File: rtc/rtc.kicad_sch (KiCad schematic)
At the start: 14 parts, among them J1 Conn_02x03_Odd_Even, J2 Conn_01x04, J3 Conn_01x04, J4 Conn_01x04, U1 PCF8563T/5_518, Y1 LFXTAL016178REEL

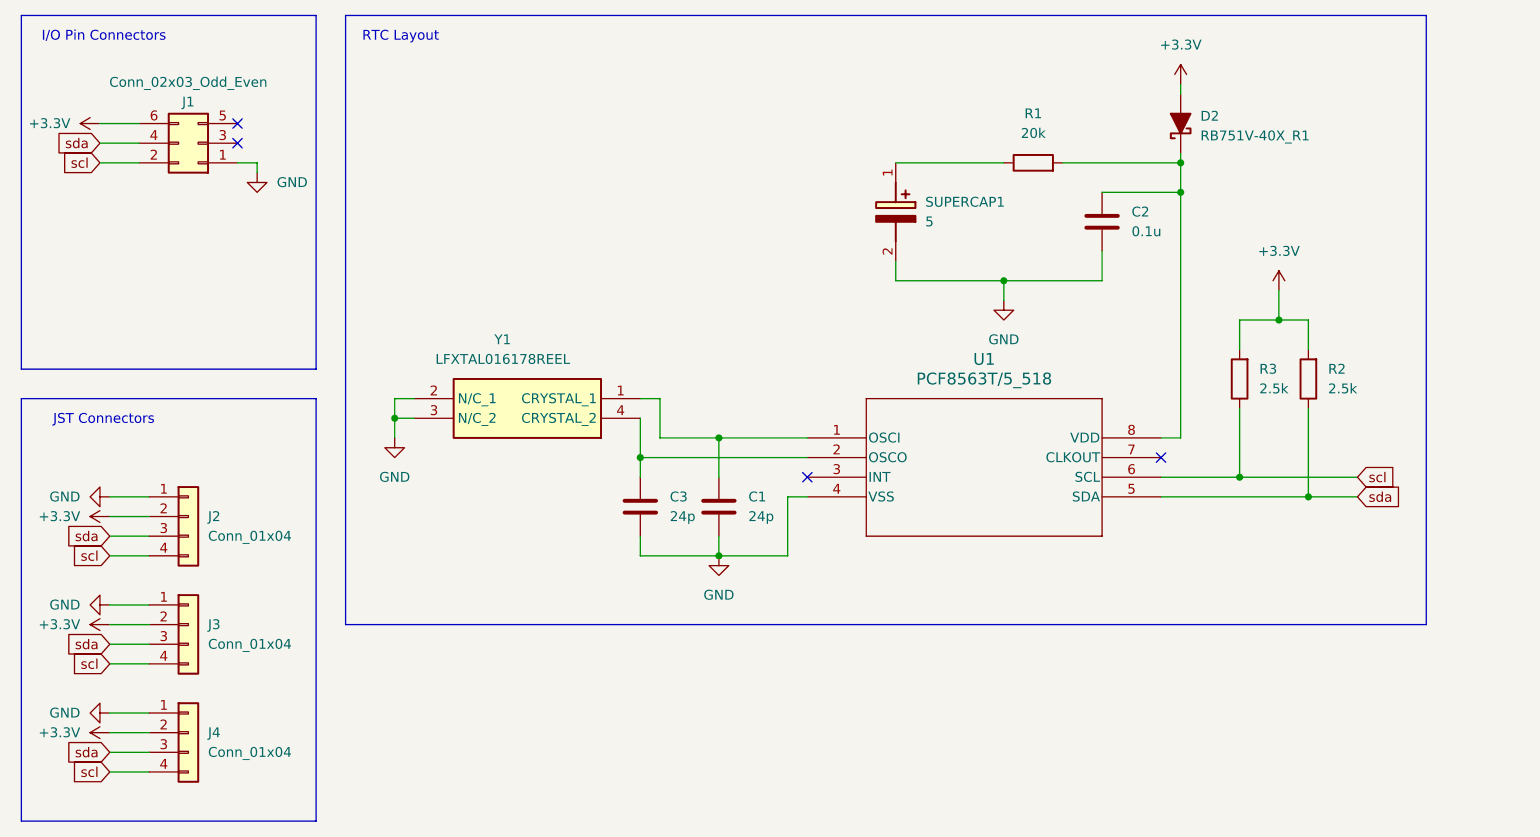
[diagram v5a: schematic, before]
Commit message: finished rtc board + sensor base 3d model change
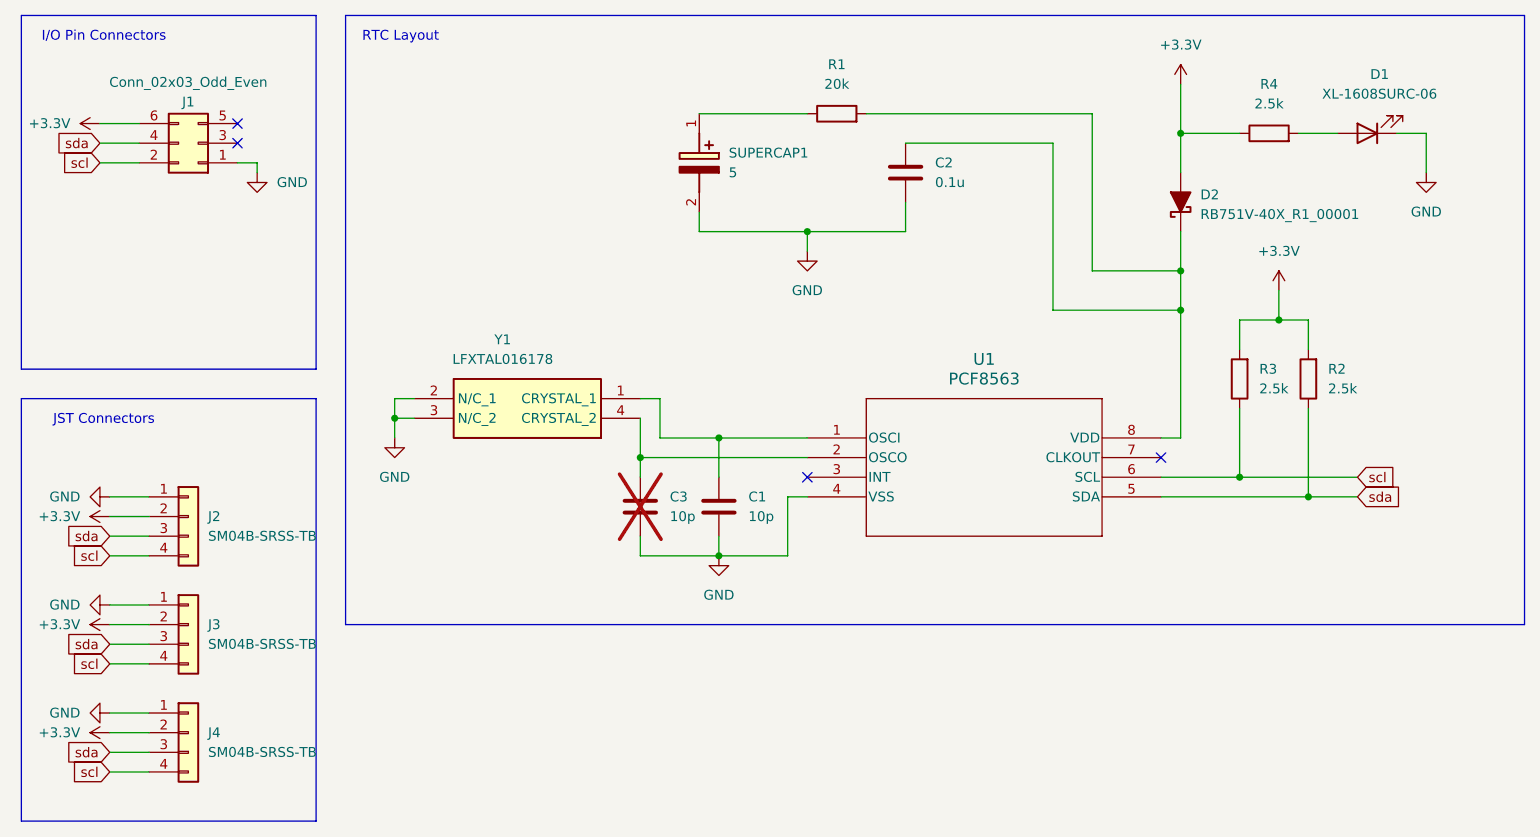
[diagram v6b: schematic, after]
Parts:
- added D1: XL-1608SURC-06, LED_SMD:LED_0603_1608Metric_Pad1.05x0.95mm_HandSolder, symbol Device:LED
- added R4: 2.5k, Resistor_SMD:R_0603_1608Metric_Pad0.98x0.95mm_HandSolder, symbol Device:R
- C1: value 24p -> 10p; footprint Capacitor_SMD:C_0402_1005Metric_Pad0.74x0.62mm_HandSolder -> Capacitor_SMD:C_0603_1608Metric_Pad1.08x0.95mm_HandSolder; Manufacturer Name (none) -> HRE; Manufacturer Part Number (none) -> CGA0603C0G100J500JT; Supplier Name (none) -> LCSC; Supplier Part Number (none) -> C45359928
- C2: footprint Capacitor_SMD:C_0402_1005Metric_Pad0.74x0.62mm_HandSolder -> Capacitor_SMD:C_0603_1608Metric_Pad1.08x0.95mm_HandSolder; Manufacturer Name (none) -> HRE; Manufacturer Part Number (none) -> CGA0603X7R104K500JT; Supplier Name (none) -> LCSC; Supplier Part Number (none) -> C6119867
- C3: value 24p -> 10p; footprint Capacitor_SMD:C_0402_1005Metric_Pad0.74x0.62mm_HandSolder -> Capacitor_SMD:C_0603_1608Metric_Pad1.08x0.95mm_HandSolder; Manufacturer Name (none) -> HRE; Manufacturer Part Number (none) -> CGA0603C0G100J500JT; Supplier Name (none) -> LCSC; Supplier Part Number (none) -> C45359928; now not fitted
- D2: value RB751V-40X_R1 -> RB751V-40X_R1_00001; Manufacturer Name (none) -> Panjit International Inc.; Manufacturer Part Number (none) -> RB751V-40X_R1_00001; Supplier Name (none) -> Digikey; Supplier Part Number (none) -> 3757-RB751V-40X_R1_00001CT-ND
- J1: now left out of the parts list
- J2, J3, J4: value Conn_01x04 -> SM04B-SRSS-TB; Manufacturer Name (none) -> XYECONN; Manufacturer Part Number (none) -> XY-SM04B-SRSS-TB; Supplier Name (none) -> LCSC; Supplier Part Number (none) -> C51940130
- R1: footprint Resistor_SMD:R_0402_1005Metric_Pad0.72x0.64mm_HandSolder -> Resistor_SMD:R_0603_1608Metric_Pad0.98x0.95mm_HandSolder; Manufacturer Name (none) -> FOJAN; Manufacturer Part Number (none) -> FRQ0603F2002TS; Supplier Name (none) -> LCSC; Supplier Part Number (none) -> C7468442
- R2, R3: footprint Resistor_SMD:R_0402_1005Metric_Pad0.72x0.64mm_HandSolder -> Resistor_SMD:R_0603_1608Metric_Pad0.98x0.95mm_HandSolder; Manufacturer Name (none) -> FOJAN; Manufacturer Part Number (none) -> FRC0603F2551TS; Substitutional Values (none) -> 2.55k; Supplier Name (none) -> LCSC; Supplier Part Number (none) -> C2933178
- SUPERCAP1: Manufacturer Name (none) -> CDA; Manufacturer Part Number (none) -> CE5R5505HF-ZJ; Manufacturer_Name CDA -> (none); Manufacturer_Part_Number CE5R5505HF-ZJ -> (none); Supplier Name (none) -> Digikey; Supplier Part Number (none) -> 4688-CE5R5505HF-ZJ-ND
- U1: value PCF8563T/5_518 -> PCF8563; Manufacturer Name (none) -> NXP; Manufacturer Part Number (none) -> PCF8563T/5,518; Supplier Name (none) -> LCSC; Supplier Part Number (none) -> C7440
- Y1: value LFXTAL016178REEL -> LFXTAL016178; Manufacturer Name (none) -> IQD; Manufacturer Part Number (none) -> LFXTAL016178; Manufacturer_Name IQD -> (none); Manufacturer_Part_Number LFXTAL016178REEL -> (none); Supplier Name (none) -> Digikey; Supplier Part Number (none) -> 1923-LFXTAL016178CT-ND
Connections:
- net +3.3V: now also R4.1
- net GND: now also D1.1 (K)
- new net: D1.2 (A), R4.2
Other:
- moved on the sheet: C2, D2, R1, SUPERCAP1

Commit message: onboarding fix
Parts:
- D1: value XL-1608SURC-06 -> LED
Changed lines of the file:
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@@
 			)
 		)
-		(property "Value" "XL-1608SURC-06"
+		(property "Value" "LED"
 			(at 208.5975 40.64 0)
 			(effects

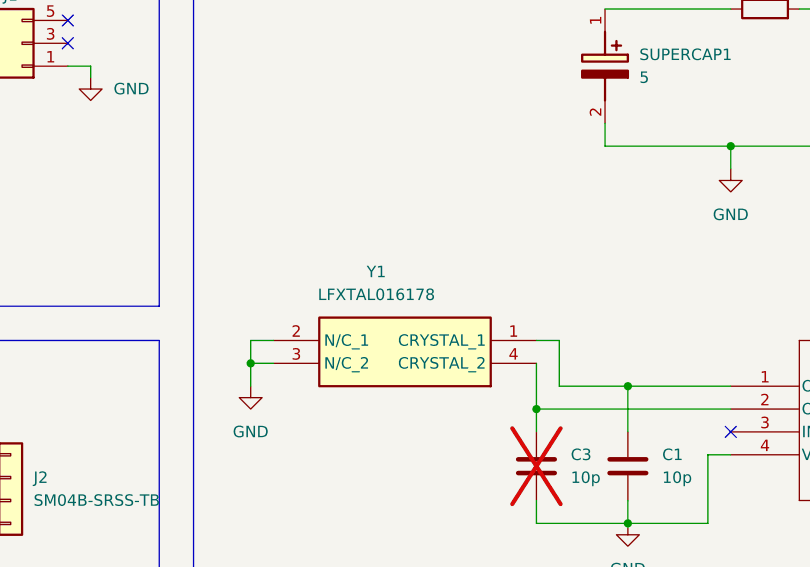
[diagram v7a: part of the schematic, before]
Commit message: updated onboarding and rtc crystal model change
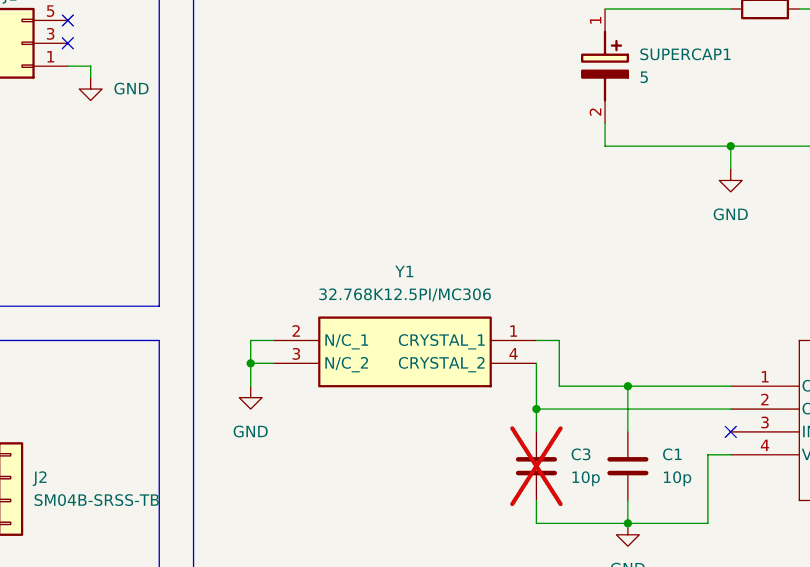
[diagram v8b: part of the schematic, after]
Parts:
- Y1: value LFXTAL016178 -> 32.768K12.5PI/MC306
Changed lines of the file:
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@@
 		(fields_autoplaced yes)
 		(property "Reference" "Y1"
-			(at 95.25 72.39 0)
+			(at 98.425 72.39 0)
 			(effects
 				(font
@@
 			)
 		)
-		(property "Value" "LFXTAL016178"
-			(at 95.25 74.93 0)
+		(property "Value" "32.768K12.5PI/MC306"
+			(at 98.425 74.93 0)
 			(effects
 				(font
